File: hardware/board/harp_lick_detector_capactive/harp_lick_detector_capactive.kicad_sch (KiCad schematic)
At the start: 54 parts

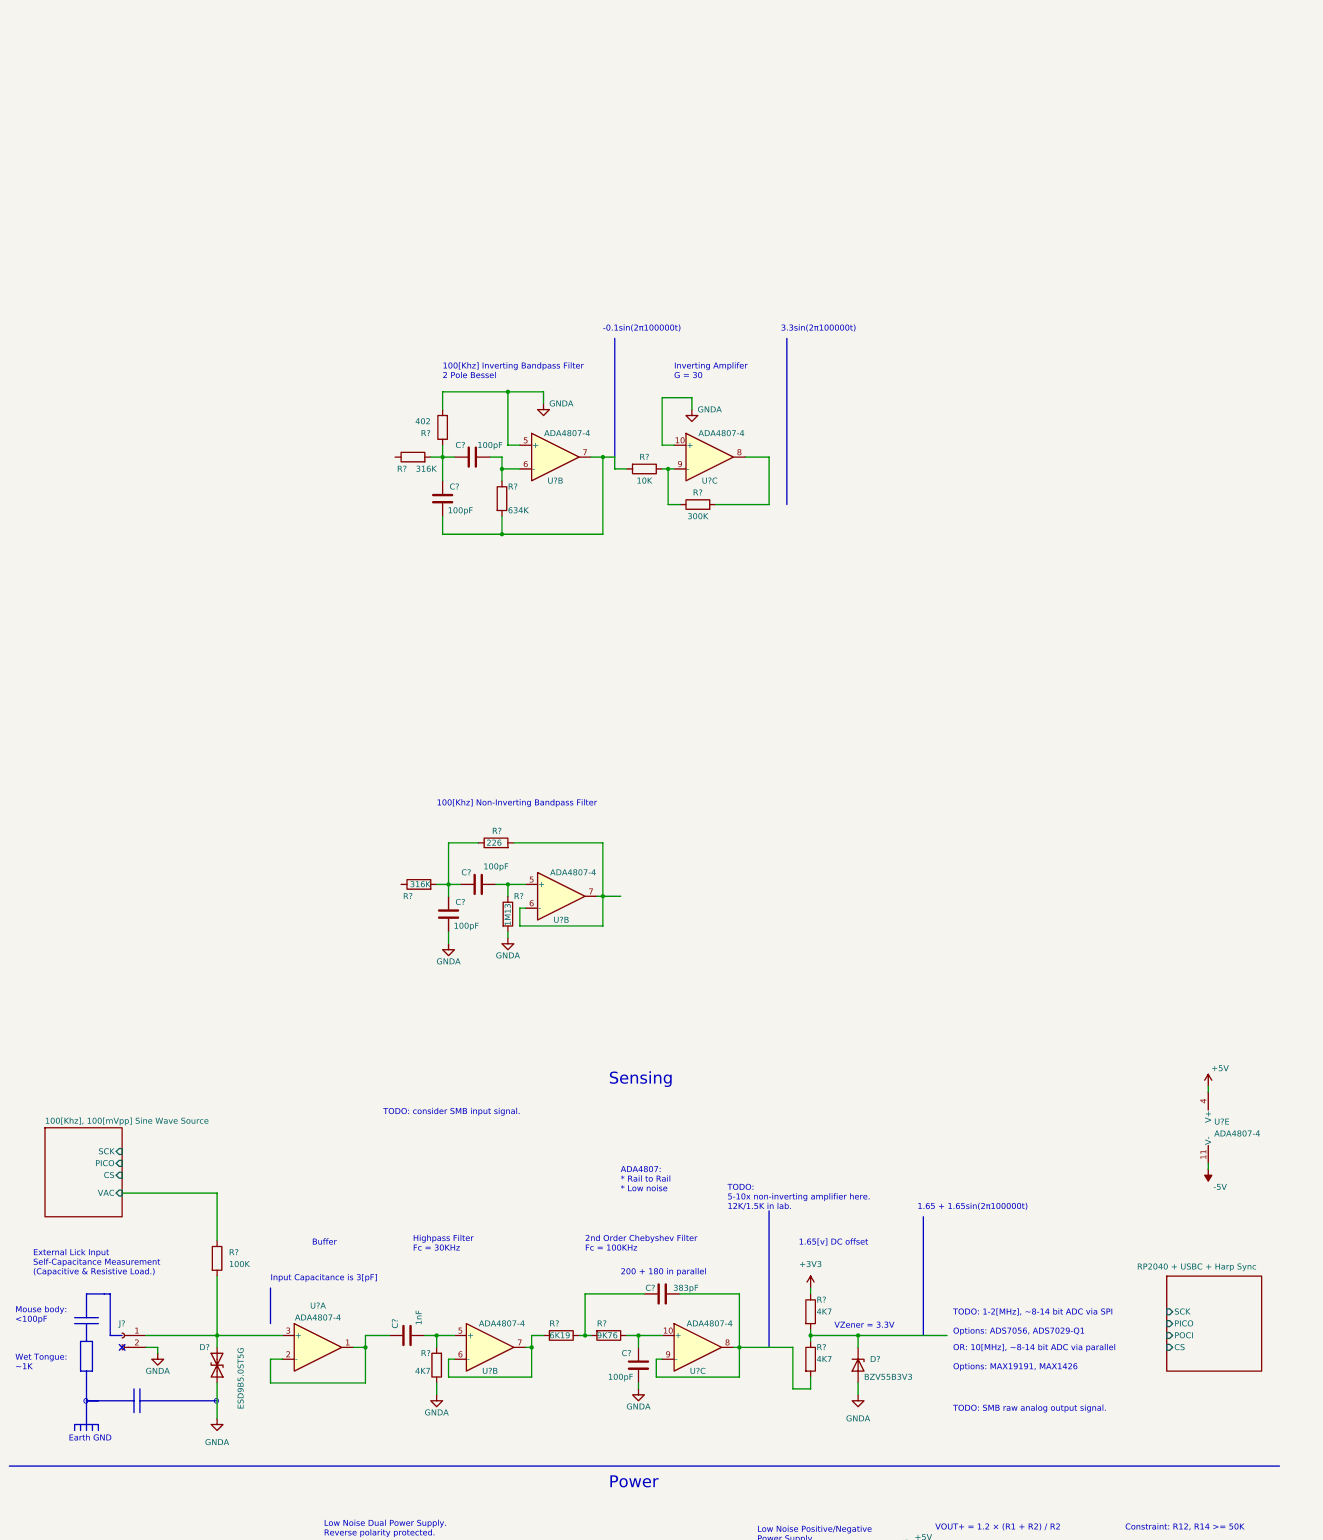
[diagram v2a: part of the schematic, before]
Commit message: draft wheatstone implementation
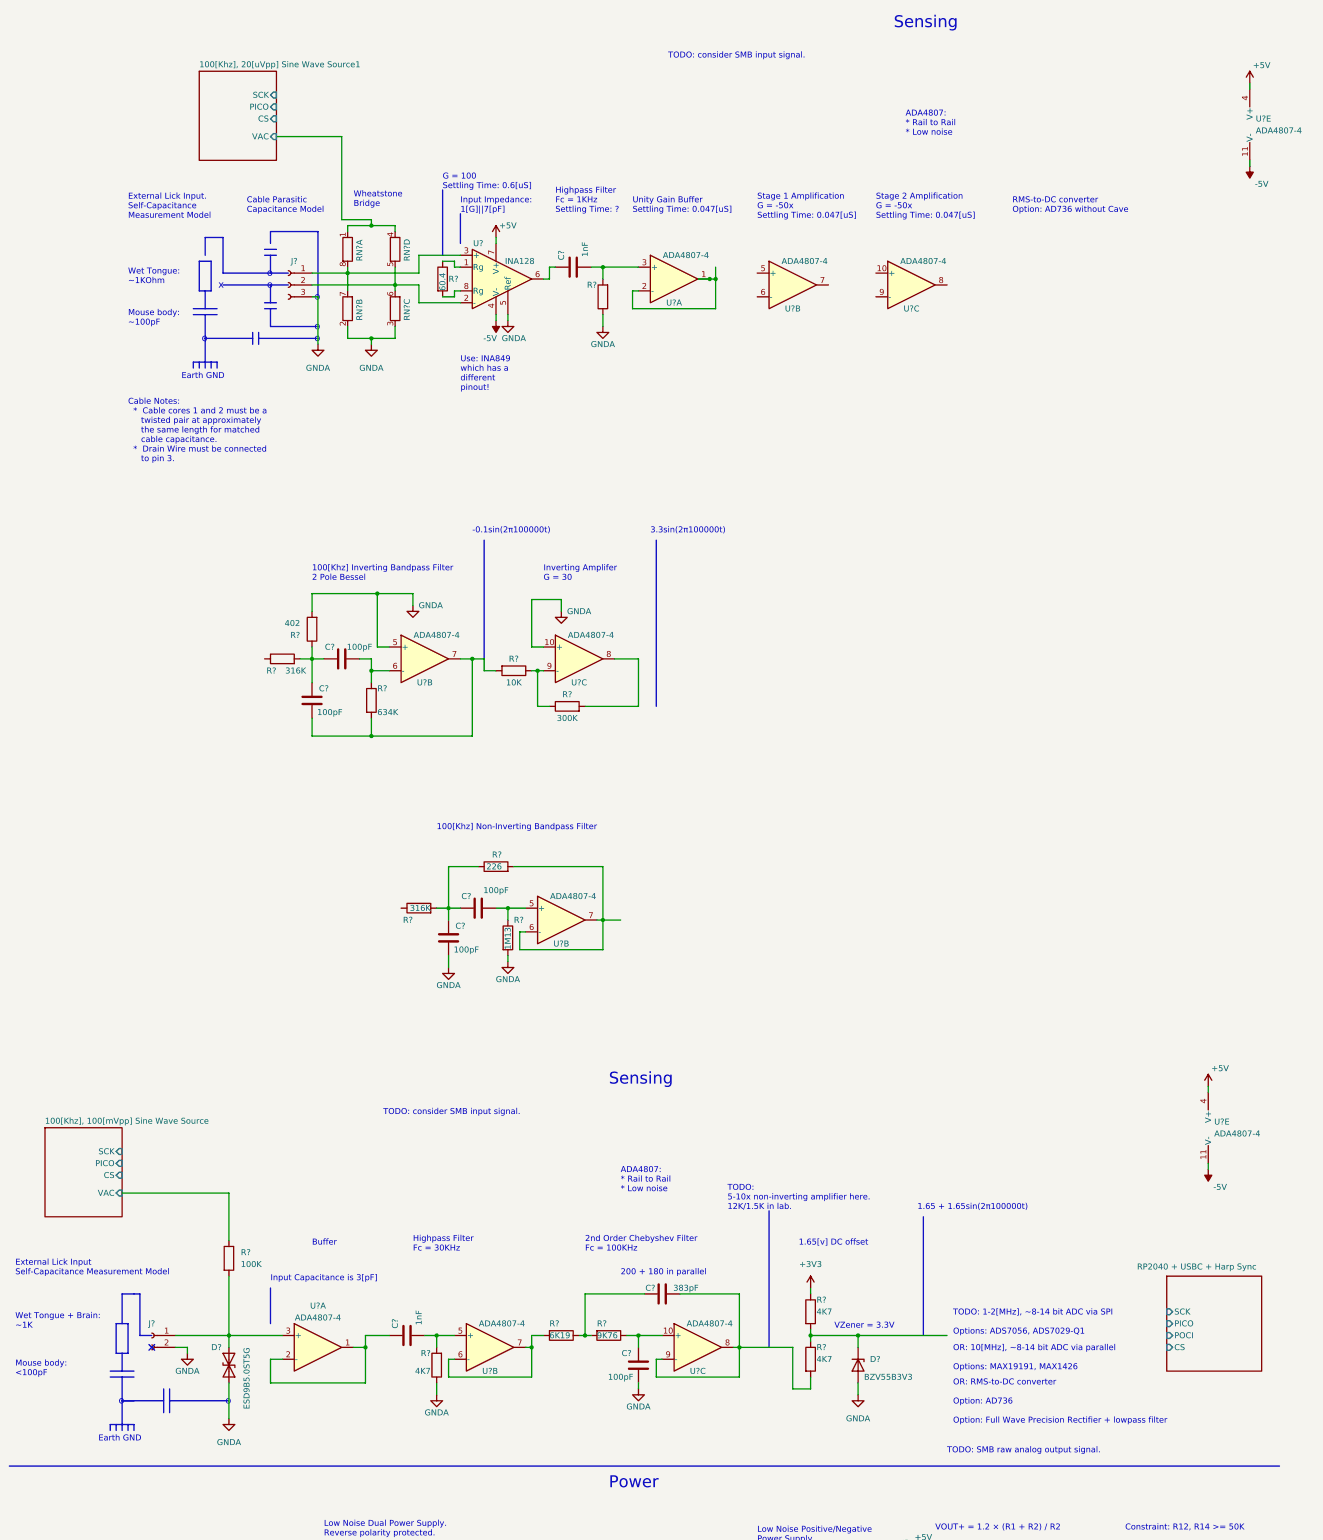
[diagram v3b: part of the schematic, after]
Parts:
- added C?: 1nF, symbol Device:C
- added J?: (no value), symbol Connector:Conn_01x03_Female
- added R?: (no value), symbol Device:R
- added R?: 60.4, symbol Device:R
- added RN? (x4): (no value), symbol Device:R_Pack04_Split
- added U? (x4): ADA4807-4, symbol Amplifier_Operational:ADA4807-4
- added U?: INA128, symbol Amplifier_Instrumentation:INA128
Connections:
- net +5V: now also U?.4 (V+), U?.7 (V+)
- net -5V: now also U?.11 (V-), U?.4 (V-)
- net GNDA: now also J?.3 (Pin_3), R?.1, RN?.2 (R2.1), RN?.3 (R3.1), U?.5 (Ref)
- new net: J?.1 (Pin_1), RN?.7 (R2.2), RN?.8 (R1.2), U?.3 (+)
- new net: U?.1, U?.2 (-)
- new net: C?.2, R?.2, U?.3 (+)
- new net: C?.1, U?.6
- new net: R?.1, U?.1 (Rg)
- new net: J?.2 (Pin_2), RN?.5 (R4.2), RN?.6 (R3.2), U?.2 (-)
- new net: R?.2, U?.8 (Rg)
- new net 100[Khz], 20[uVpp] Sine Wave Source1/VAC: RN?.1 (R1.1), RN?.4 (R4.1)
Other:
- added sheet 100[Khz], 20[uVpp] Sine Wave Source1 (sine_wave_source.kicad_sch)
- note added: "Cable Notes: * Cable cores 1 and 2 must be a twisted pair at approximately the same length for matched cable capacitance. * Drain Wire must be connected to pin 3."
- note added: "Cable Parasitic Capacitance Model"
- note added: "External Lick Input Self-Capacitance Measurement Model"
- note added: "External Lick Input. Self-Capacitance Measurement Model"
- note added: "G = 100 Settling Time: 0.6[uS]"
- note added: "Highpass Filter Fc = 1KHz Settling Time: ?"
- note added: "Input Impedance: 1[G]||7[pF]"
- note added: "Mouse body: ~100pF"
- note added: "OR: RMS-to-DC converter Option: AD736 Option: Full Wave Precision Rectifier + lowpass filter"
- note added: "RMS-to-DC converter Option: AD736 without Cave"
- note added: "Stage 1 Amplification G = -50x Settling Time: 0.047[uS]"
- note added: "Stage 2 Amplification G = -50x Settling Time: 0.047[uS]"
- note added: "Unity Gain Buffer Settling Time: 0.047[uS]"
- note added: "Use: INA849 which has a different pinout!"
- note added: "Wet Tongue + Brain: ~1K"
- note added: "Wet Tongue: ~1KOhm"
- note added: "Wheatstone Bridge"
- note added: "x"
- note removed: "External Lick Input Self-Capacitance Measurement (Capacitive & Resistive Load.)"
- note removed: "Wet Tongue: ~1K"
- moved on the sheet: C?, D?, J?, R?, U?B, U?C

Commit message: update analog front end
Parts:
- removed U?: INA128, symbol Amplifier_Instrumentation:INA128
- added C? (x2): (no value), symbol Device:C
- added C?: 100pF, symbol Device:C
- added D?: BZV55B3V3, Diode_SMD:D_MiniMELF, symbol Diode:BZV55B3V3
- added J?: (no value), symbol Connector:Conn_Coaxial
- added R?: 6K19, symbol Device:R
- added R?: 9K76, symbol Device:R
- added R? (x2): (no value), symbol Device:R
- added R? (x2): 4K7, symbol Device:R
- added RV?: (no value), symbol Device:R_Potentiometer_Trim
- added unit 4 of U1
- added U?: INA849, symbol machine_agency_components:INA849
- C?: value 1uF -> (none); Notes (none) -> must not be polarized
- C? (x5): value ??? -> (none)
- J?: value (none) -> Conn_01x03_Female
- R?: value 10k -> (none)
- R?: value (none) -> 10K
- U?: value LT3030 -> (none)
- gave numbers to parts that had none: 1
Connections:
- net GNDA is gone; now on net GND: C?.2, C?.2, C?.2, C?.2, C?.2, D?.1 (A1), D?.2 (A), J?.2 (Pin_2), J?.3 (Pin_3), R12.2, R14.2, R?.1, R?.1, R?.2, R?.2, RN?.2 (R2.1), RN?.3 (R3.1), U?.10 (+), U?.13 (PAD), U?.4 (GND), U?.5 (+)
- net +3V3: now also R?.1
- net +5V: now also U?.8 (V+)
- net -5V: now also U?.5 (V-)
- net GND: now also U1.3 (+), C?.2, C?.2, D?.2 (A), J?.2 (Ext), U?.6 (Ref)
- net at U1.10 (+): now also C?.2, R?.2
- net at U1.8: now also U1.9 (-), R?.2
- net at U1.5 (+): now also C?.1, R?.1
- net at U1.6 (-): now also U1.7, C?.1, R?.2
- net at J?.1 (Pin_1), RN?.7 (R2.2), RN?.8 (R1.2): now also U?.4 (+)
- net at U1.1: now also J?.1 (In), R?.2, RV?.2; no longer U1.2 (-)
- net at C?.1: now also U?.7
- net at R?.1: now also U?.2 (Rg)
- net at J?.2 (Pin_2), RN?.5 (R4.2), RN?.6 (R3.2): now also U?.1 (-)
- net at R?.2: now also U?.3 (Rg)
- net 100[Khz], 50[uVpp] Sine Wave Source1/VAC renamed 100[Khz], 50[uVpp] Sine Wave Source1/VSIN
- new net: R?.2, RV?.1, U1.2 (-)
- new net: C?.2, R?.1, R?.2
- new net: C?.1, R?.1, U1.12 (+)
- new net: R?.1, U1.13 (-), U1.14
- new net MCU/ADC: D?.1 (K), R?.1, R?.2
- no-connect marks 2 -> 3
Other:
- sheet 100[Khz], 20[uVpp] Sine Wave Source1 renamed 100[Khz], 50[uVpp] Sine Wave Source1
- sheet RP2040 + USBC + Harp Sync renamed MCU
- sheet 100[Khz], 50[uVpp] Sine Wave Source1 ports: added VSIN; removed VAC
- sheet MCU ports: added ADC; removed POCI
- note added: "100K"
- note added: "2nd Order Chebyshev Filter Fc = 100KHz Settling Time: 4[us]"
- note added: "Buffer Settling Time: 0.047[us]"
- note added: "Cable Notes: * Cable cores 1 and 2 must be a twisted pair at approximately the same length for matched cable capacitance. * Shield drain wire must be connected to pin 3."
- note added: "G = -250x Settling Time: 0.047[us]"
- note added: "G = 100 Settling Time: 0.6[us]"
- note added: "Highpass Filter Fc = 15KHz Settling Time: ?"
- note added: "LEFT SIDE WORKS"
- note added: "SMB Raw Signal"
- note added: "Target: 383pF"
- note removed: "Cable Notes: * Cable cores 1 and 2 must be a twisted pair at approximately the same length for matched cable capacitance. * Drain Wire must be connected to pin 3."
- note removed: "G = 100 Settling Time: 0.6[uS]"
- note removed: "Highpass Filter Fc = 1KHz Settling Time: ?"
- note removed: "RMS-to-DC converter Option: AD736 without Cave"
- note removed: "Stage 1 Amplification G = -50x Settling Time: 0.047[uS]"
- note removed: "Stage 2 Amplification G = -50x Settling Time: 0.047[uS]"
- note removed: "Unity Gain Buffer Settling Time: 0.047[uS]"
- note removed: "Use: INA849 which has a different pinout!"
- moved on the sheet: C?, D?, J?, R12, R14, R?, RN?A, RN?B, RN?C, RN?D, U1A, U1B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

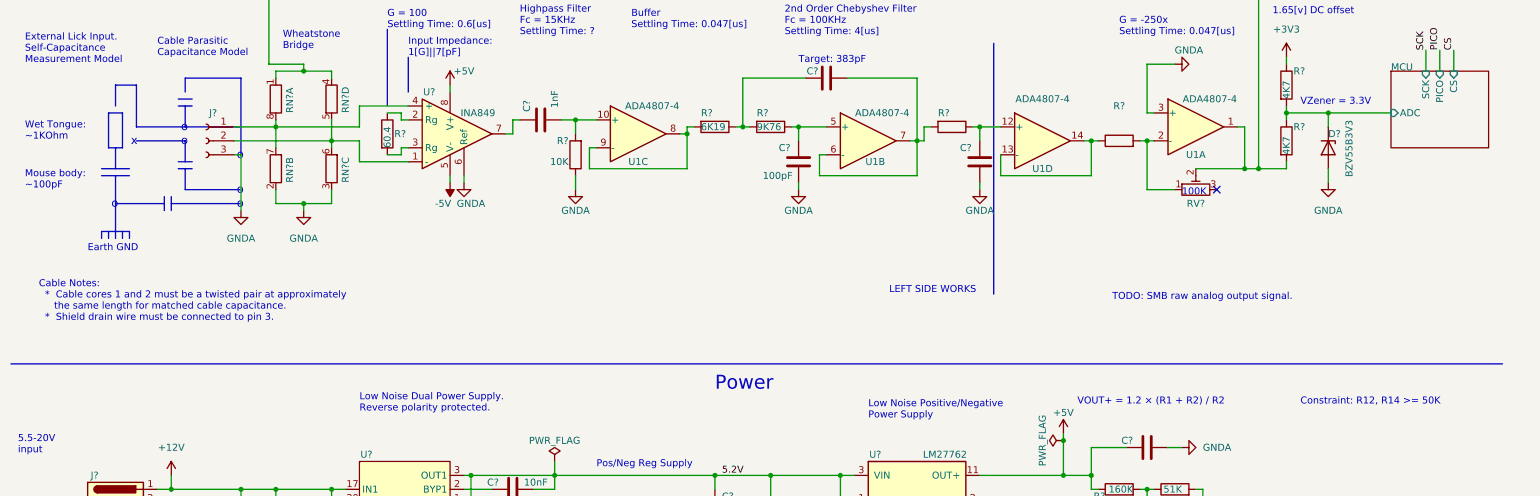
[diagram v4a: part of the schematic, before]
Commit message: update sine wave generator
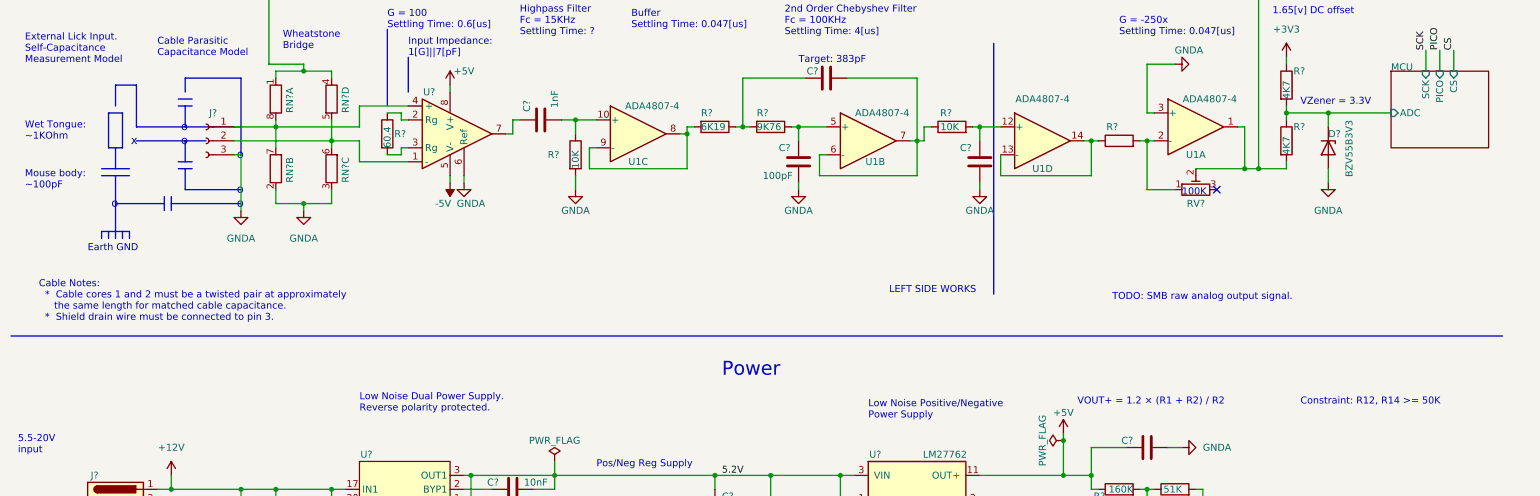
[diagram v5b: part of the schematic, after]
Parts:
- removed R?: (no value), symbol Device:R
- removed R?: 10K, symbol Device:R
- added R? (x2): 10K, Resistor_SMD:R_0402_1005Metric_Pad0.72x0.64mm_HandSolder, symbol Device:R
- R?: Link (none) -> https://www.digikey.com/en/products/detail/koa-speer-electr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
- U?: value INA849 -> (none); Link (none) -> https://www.digikey.com/en/products/detail/texas-instrument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
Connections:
- net GND: now also R?.2
- net at C?.2, U1.10 (+): now also R?.1
- net at C?.1, U1.6 (-), U1.7: now also R?.1
- net at C?.1, U1.12 (+): now also R?.2
